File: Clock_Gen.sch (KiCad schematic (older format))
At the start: 37 parts

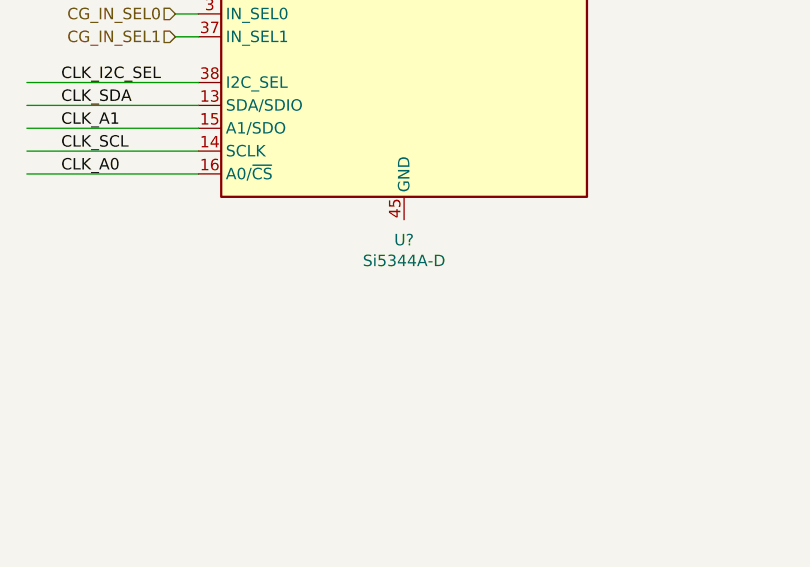
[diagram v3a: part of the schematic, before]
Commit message: -Clock --GND pin was missing. it was added to pin 45 -BTB --pins added
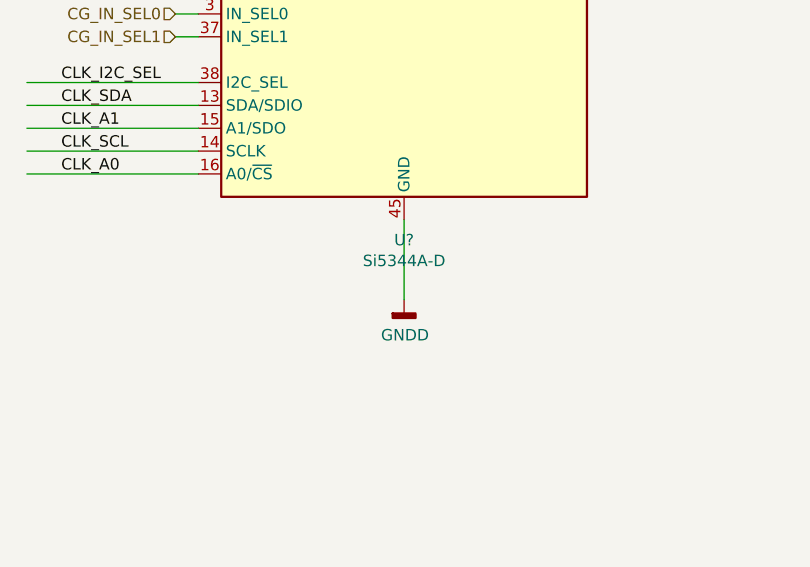
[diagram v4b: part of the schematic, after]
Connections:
- wire segments 163 -> 164
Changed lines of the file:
@@
 Wire Wire Line
 	5300 4050 6450 4050
+$Comp
+L power:GNDD #PWR?
+U 1 1 6064F5D7
+P 7350 5800
+AR Path="/601DF0A6/6064F5D7" Ref="#PWR?"  Part="1"
+AR Path="/601E7C5A/6064F5D7" Ref="#PWR?"  Part="1"
+AR Path="/601E7CC8/6064F5D7" Ref="#PWR?"  Part="1"
+AR Path="/601E7C92/6064F5D7" Ref="#PWR?"  Part="1"
+AR Path="/601E7C92/60257FE5/6064F5D7" Ref="#PWR?"  Part="1"
+AR Path="/601E7B38/6064F5D7" Ref="#PWR?"  Part="1"
+AR Path="/601E7BBE/6064F5D7" Ref="#PWR?"  Part="1"
+F 0 "#PWR?" H 7350 5550 50  0001 C CNN
+F 1 "GNDD" H 7354 5645 50  0000 C CNN
+F 2 "" H 7350 5800 50  0001 C CNN
+F 3 "" H 7350 5800 50  0001 C CNN
+	1    7350 5800
+	1    0    0    -1
+$EndComp
+Wire Wire Line
+	7350 5450 7350 5800
 $EndSCHEMATC

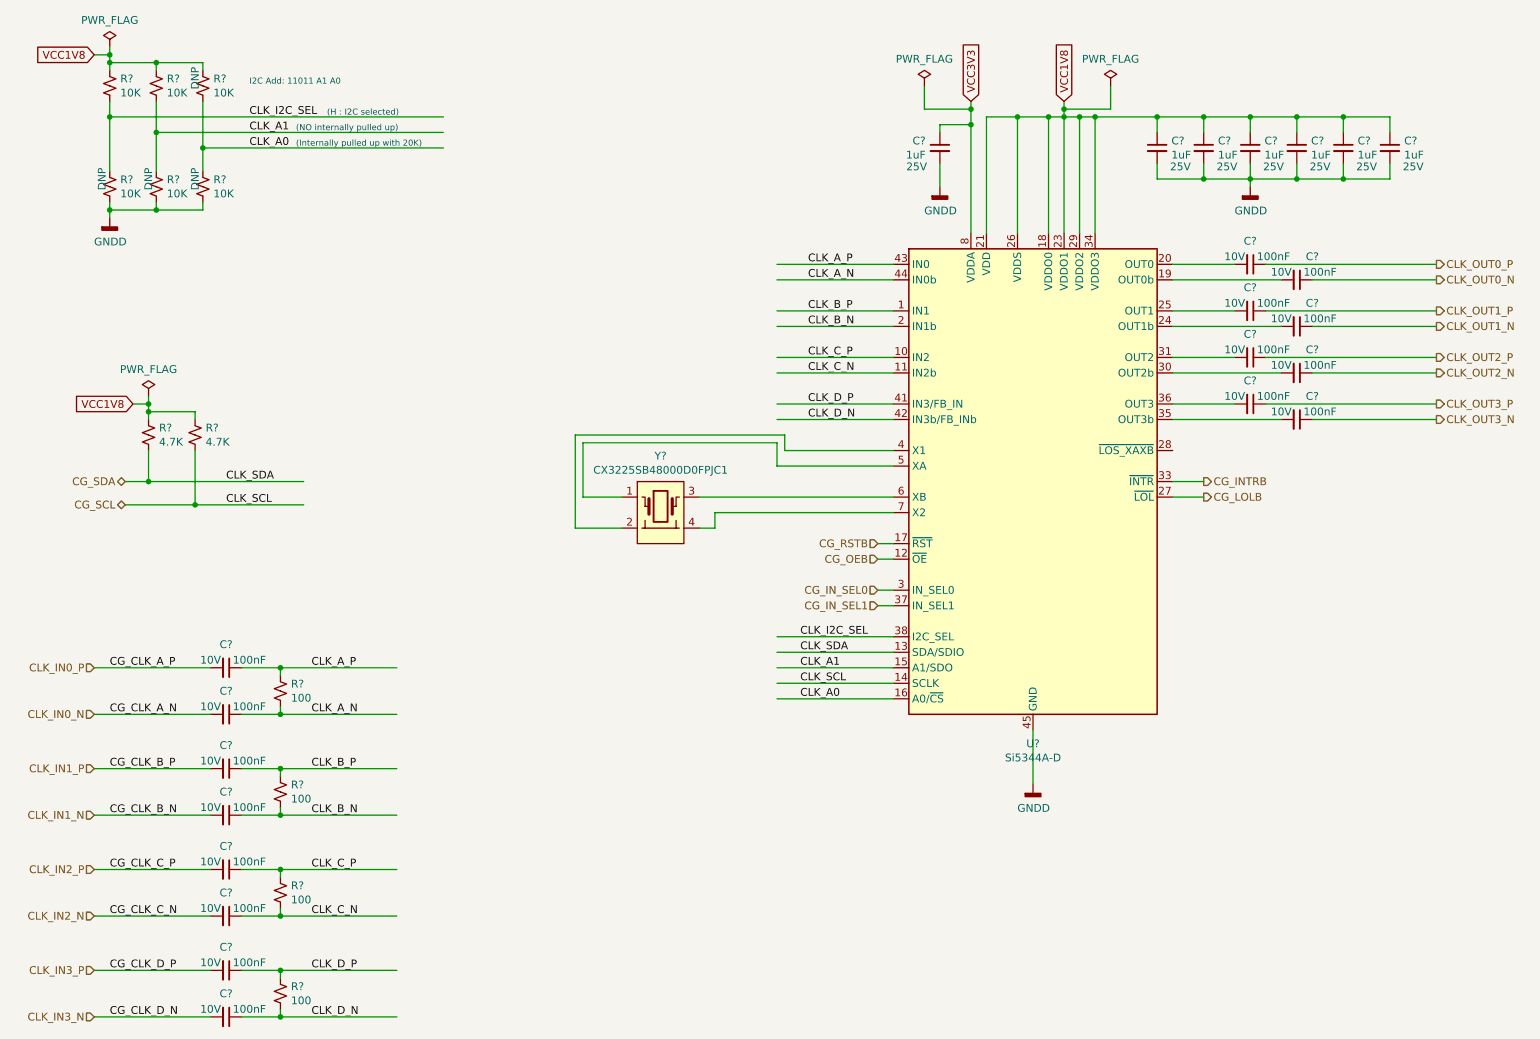
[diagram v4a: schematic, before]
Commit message: PCB created and schematics annotated High speed connections added to the BTB
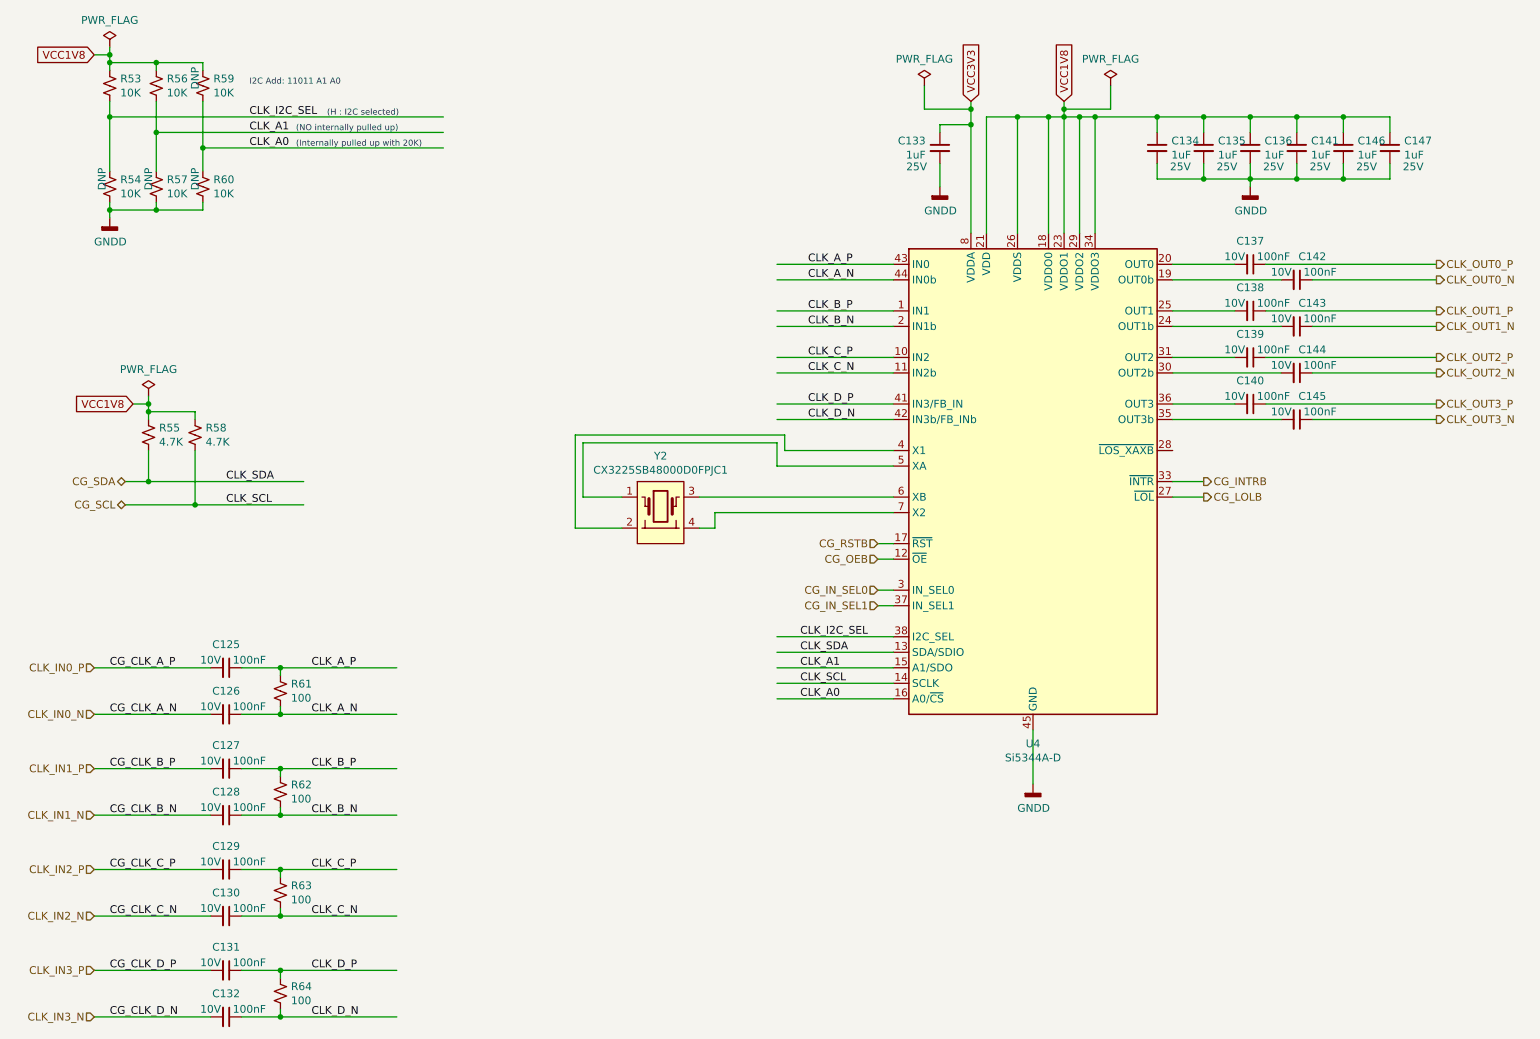
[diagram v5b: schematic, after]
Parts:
- gave numbers to parts that had none: 37

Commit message: Corrected PCB import errors
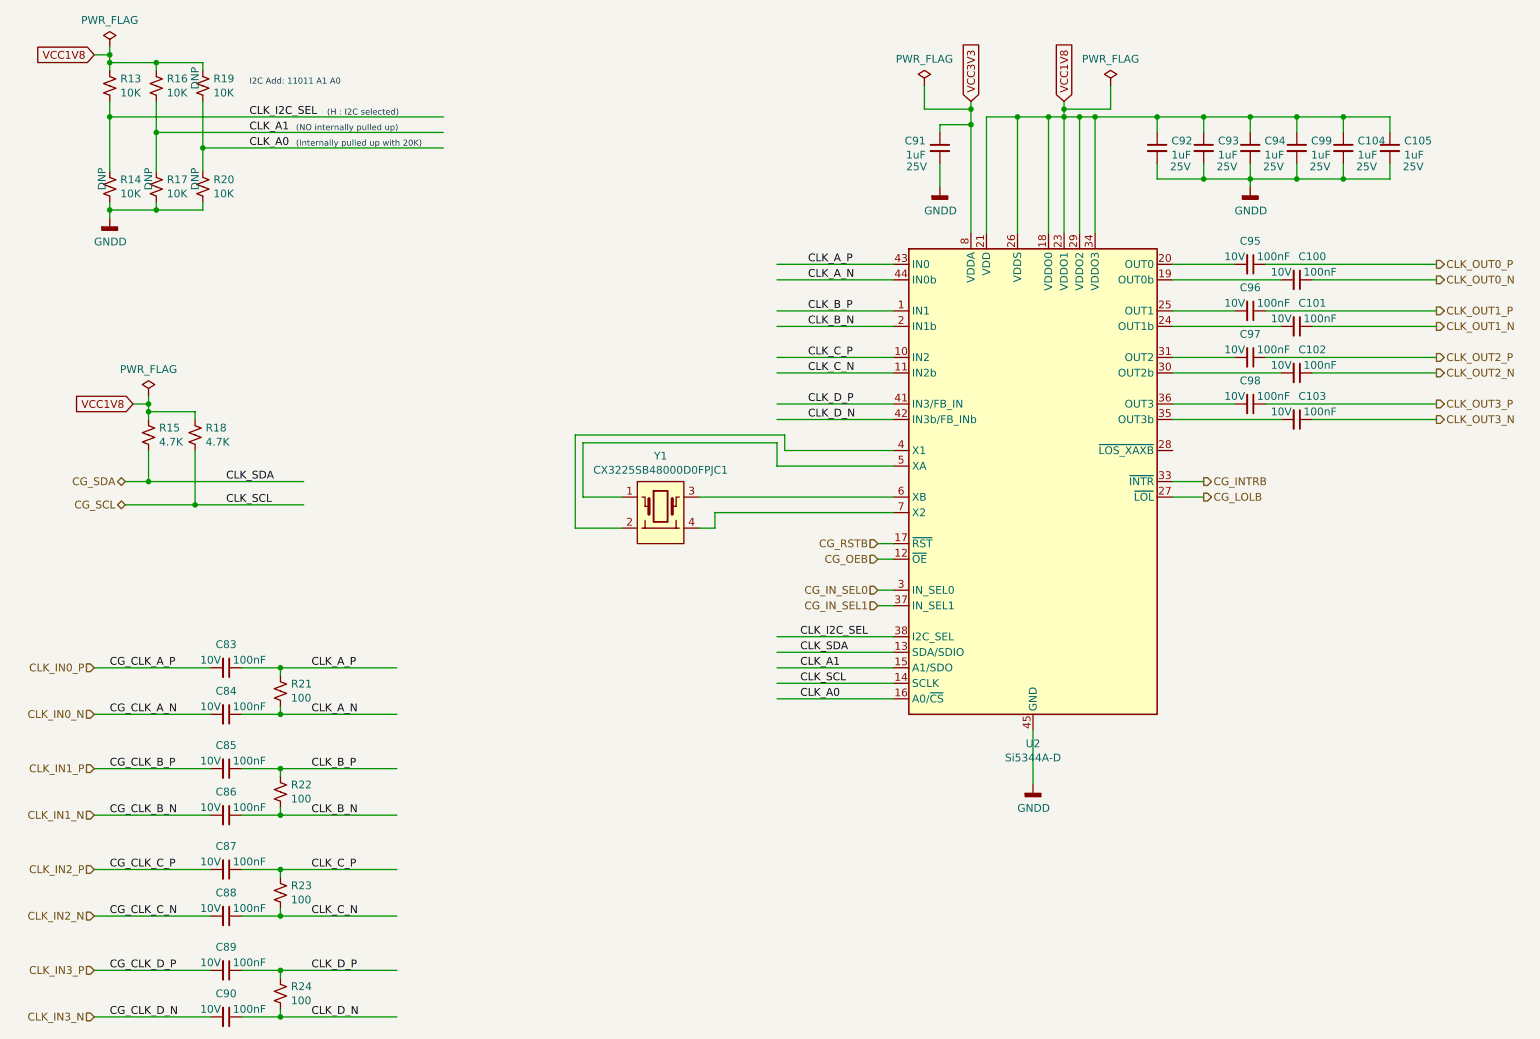
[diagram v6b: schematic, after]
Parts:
- renumbered C142 to C100, C143 to C101, C144 to C102, C145 to C103, C146 to C104, C147 to C105, C125 to C83, C126 to C84, C127 to C85, C128 to C86, C129 to C87, C130 to C88, C131 to C89, C132 to C90, C133 to C91, C134 to C92, C135 to C93, C136 to C94, C137 to C95, C138 to C96, C139 to C97, C140 to C98, C141 to C99, R53 to R13, R54 to R14, R55 to R15, R56 to R16, R57 to R17, R58 to R18, R59 to R19, R60 to R20, R61 to R21, R62 to R22, R63 to R23, R64 to R24, U4 to U2, Y2 to Y1
